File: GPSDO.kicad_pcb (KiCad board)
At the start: 2 copper layers, 85 x 85 mm, 100 parts, among them J1 Conn_Coaxial, J10 Conn_Coaxial, J2 Barrel_Jack, J3 PROG, J4 DISP_MODULE, J5 GPS_CONN, J6 Conn_Coaxial, J7 Conn_Coaxial, J8 Conn_Coaxial, J9 Conn_Coaxial, SW1 RESET_BTN, U1 REF3440IDBVR, U10 AVR32DB28x-xSO, U11 AZ1117H-5.0TRG1, U12 AZ1117H-5.0TRG1, U13 74HC390, U14 DS34C87T, U15 MCP6486T-E/OT, U2 74AUC2G04, U3 74AUC2G04, U4 74LVC2G74DP,125, U5 AD5680, U6 NB3N551MN, U7 74LVC1G125SE-7, U8 74LVC1G125SE-7, U9 LTC2050IS8, X1 OC5SC25

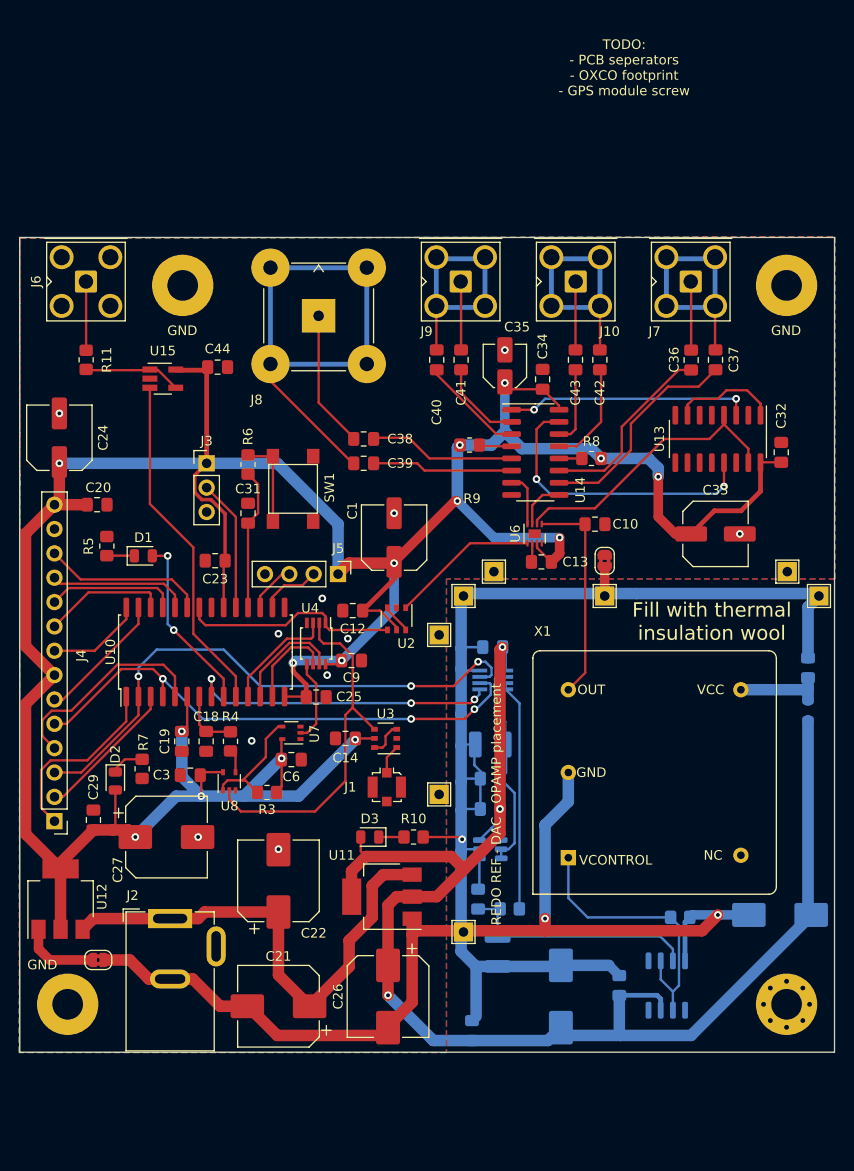
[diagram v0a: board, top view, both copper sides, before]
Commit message: changed flipflop & added vref
Flip-flop doesn't really benefit from having a set/reset that can be changed.
uC benefits from having an external reference. If not placed, internal one can be used.
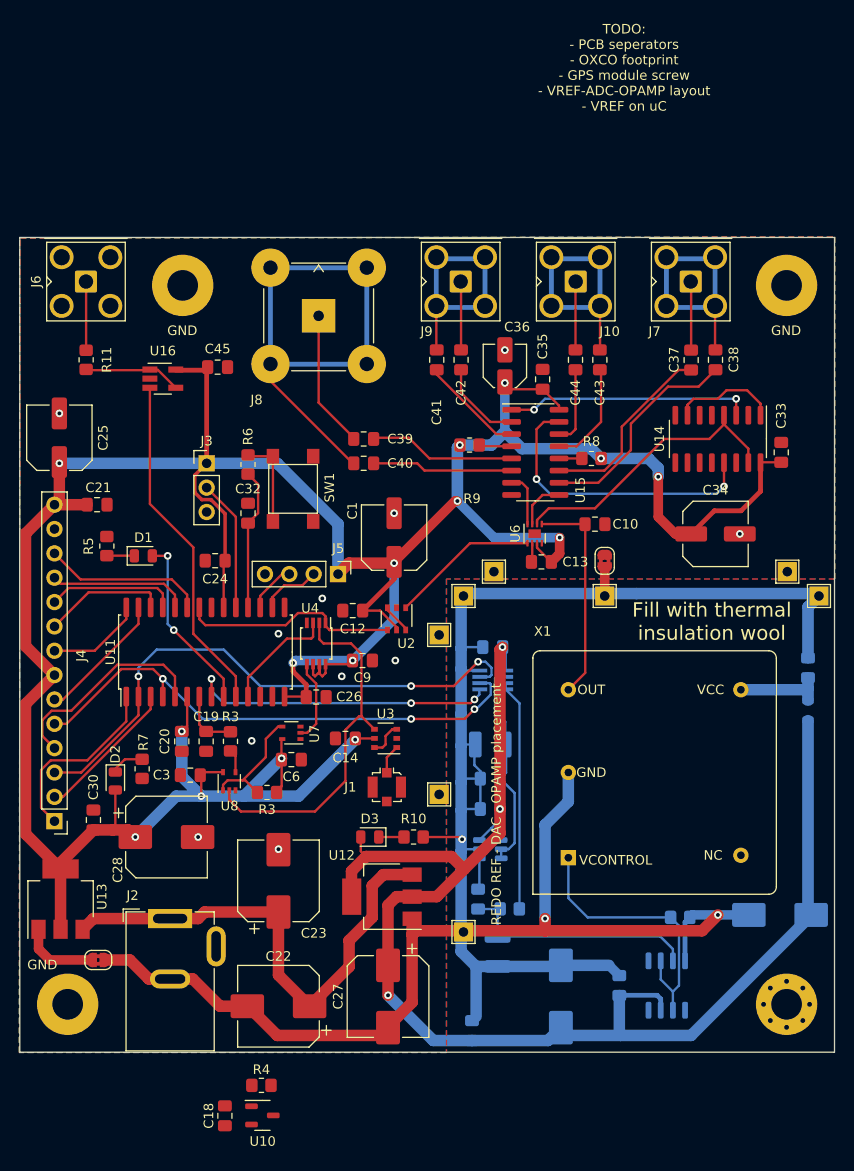
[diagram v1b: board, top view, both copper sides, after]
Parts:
- added C18: 10n, Capacitor_SMD:C_0805_2012Metric_Pad1.18x1.45mm_HandSolder, F.Cu at (41.4, 111.6)
- added R4: 270R, Resistor_SMD:R_0805_2012Metric_Pad1.20x1.40mm_HandSolder, F.Cu at (45.2, 108.5)
- added U10: LM4040AEX3-3.3+T, Package_TO_SOT_SMD:SOT-23-3, F.Cu at (45.3, 111.6)
- moved C9 1.14 mm to (55.8, 64.1)
- renumbered C18 to C19, C19 to C20, C20 to C21, C21 to C22, C22 to C23, C23 to C24, C24 to C25, C25 to C26, C26 to C27, C27 to C28, C28 to C29, C29 to C30, C30 to C31, C31 to C32, C32 to C33, C33 to C34, C34 to C35, C35 to C36, C36 to C37, C37 to C38, C38 to C39, C39 to C40, C40 to C41, C41 to C42, C42 to C43, C43 to C44, C44 to C45, R4 to R3, U10 to U11, U11 to U12, U12 to U13, U13 to U14, U14 to U15, U15 to U16
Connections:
- U11 pad 12: /FF_SET -> /UNUSED
- U11 pad 13: /FF_RESET -> /VREF_3V3
- U4 pad 6: /FF_RESET -> +5VD
- U4 pad 7: /FF_SET -> +5VD
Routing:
- net /FF_SET: track 11.6 -> 0.00 mm
- net /FF_RESET: track 9.66 -> 0.00 mm
- net +5VD: track 331.6 -> 338.7 mm
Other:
- board text added: "TODO: - PCB seperators - OXCO footprint - GPS module screw - VREF-ADC-OPAMP layout - VREF on uC"
- board text removed: "TODO: - PCB seperators - OXCO footprint - GPS module screw"

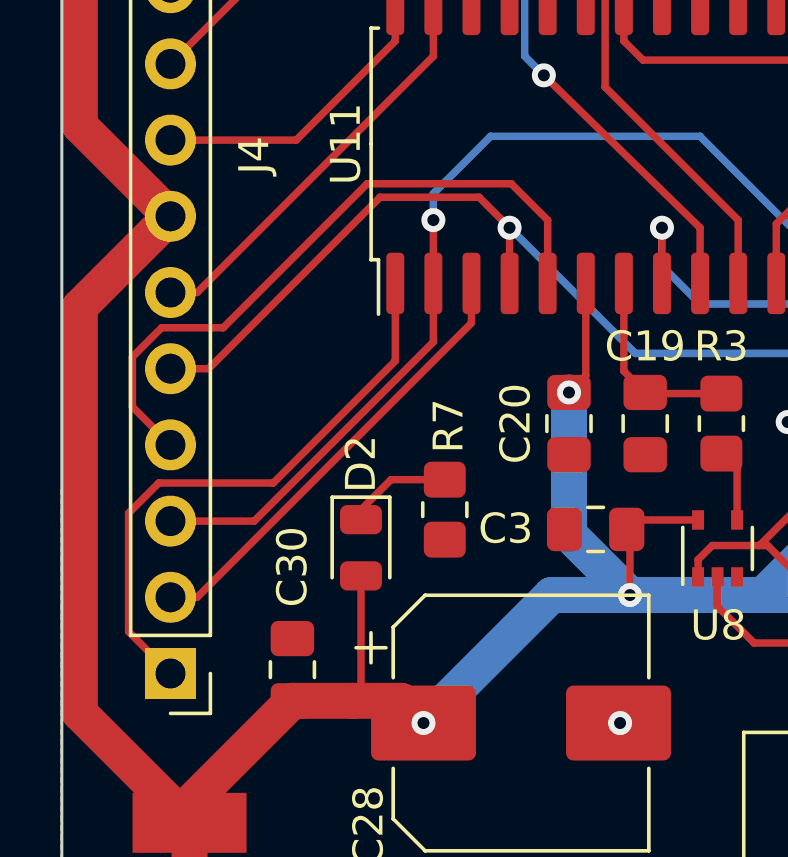
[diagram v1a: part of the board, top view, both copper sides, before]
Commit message: updated LCD layout
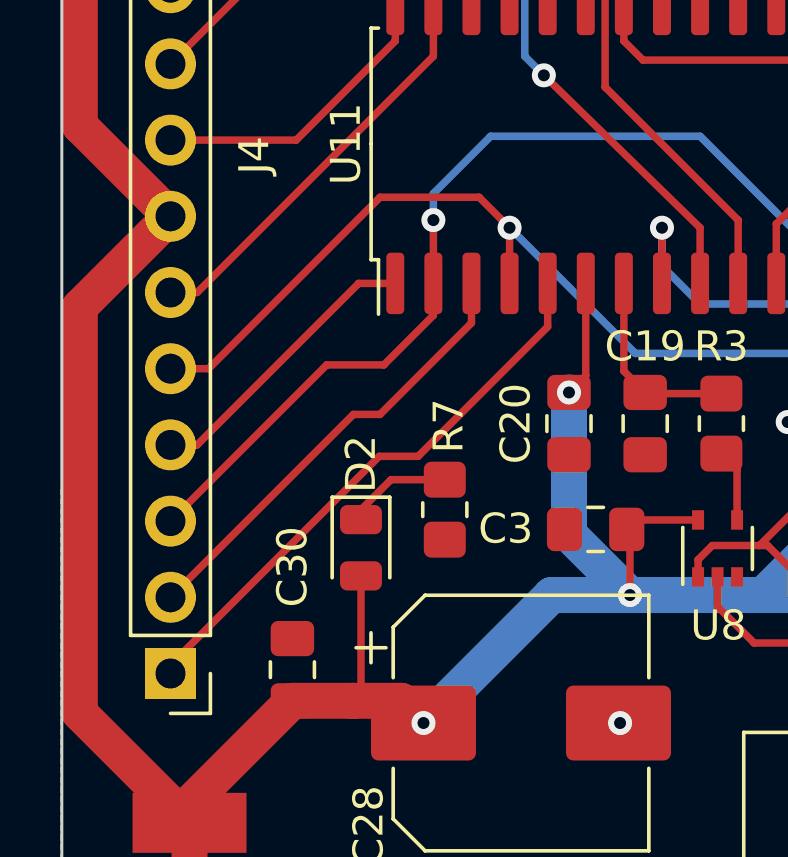
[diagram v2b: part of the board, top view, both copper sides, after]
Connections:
- U11 pad 1: /TOUCH_IRQ -> /~{TOUCH_SS}
- U11 pad 5: /~{TOUCH_SS} -> /TOUCH_IRQ
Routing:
- net /~{TOUCH_SS}: track 22.3 -> 9.72 mm
- net /TOUCH_IRQ: track 19.5 -> 19.0 mm
- net /DAC_MOSI: track 58.7 -> 58.2 mm
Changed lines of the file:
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@@
     (fp_line (start -2.75 -8.95) (end 3.75 -8.95) (layer "F.Fab") (width 0.1))
     (pad "1" smd roundrect (at -4.65 -8.255 90) (size 2.05 0.6) (layers "F.Cu" "F.Paste" "F.Mask") (roundrect_rratio 0.25)
-      (net 52 "/TOUCH_IRQ") (pinfunction "PA7") (pintype "bidirectional"))
+      (net 41 "/~{TOUCH_SS}") (pinfunction "PA7") (pintype "bidirectional"))
     (pad "2" smd roundrect (at -4.65 -6.985 90) (size 2.05 0.6) (layers "F.Cu" "F.Paste" "F.Mask") (roundrect_rratio 0.25)
       (net 26 "/DAC_MOSI") (pinfunction "PC0") (pintype "bidirectional"))
@@
       (net 42 "/DAC_SCK") (pinfunction "PC2") (pintype "bidirectional"))
     (pad "5" smd roundrect (at -4.65 -3.175 90) (size 2.05 0.6) (layers "F.Cu" "F.Paste" "F.Mask") (roundrect_rratio 0.25)
-      (net 41 "/~{TOUCH_SS}") (pinfunction "PC3") (pintype "bidirectional"))
+      (net 52 "/TOUCH_IRQ") (pinfunction "PC3") (pintype "bidirectional"))
     (pad "6" smd roundrect (at -4.65 -1.905 90) (size 2.05 0.6) (layers "F.Cu" "F.Paste" "F.Mask") (roundrect_rratio 0.25)
       (net 9 "+5VD") (pinfunction "VDDIO2") (pintype "power_in"))
@@
   (segment (start 65.278 66.802) (end 67.818 64.262) (width 0.25) (layer "F.Cu") (net 26))
   (segment (start 60.833 66.802) (end 65.278 66.802) (width 0.25) (layer "F.Cu") (net 26))
+  (segment (start 28.829 70.612) (end 30.734 70.612) (width 0.25) (layer "F.Cu") (net 26))
+  (segment (start 32.385 68.961) (end 32.385 67.896) (width 0.25) (layer "F.Cu") (net 26))
   (segment (start 32.385 67.896) (end 32.385 65.786) (width 0.25) (layer "F.Cu") (net 26))
-  (segment (start 32.385 67.896) (end 32.385 69.848604) (width 0.25) (layer "F.Cu") (net 26))
-  (segment (start 32.385 69.848604) (end 26.414604 75.819) (width 0.25) (layer "F.Cu") (net 26))
-  (segment (start 26.414604 75.819) (end 23.622 75.819) (width 0.25) (layer "F.Cu") (net 26))
+  (segment (start 23.622 75.819) (end 28.829 70.612) (width 0.25) (layer "F.Cu") (net 26))
+  (segment (start 30.734 70.612) (end 32.385 68.961) (width 0.25) (layer "F.Cu") (net 26))
   (via (at 67.818 64.262) (size 0.8) (drill 0.4) (layers "F.Cu" "B.Cu") (net 26))
   (via (at 60.833 66.802) (size 0.8) (drill 0.4) (layers "F.Cu" "B.Cu") (net 26))
@@
   (segment (start 42.545 49.149) (end 42.545 58.596) (width 0.25) (layer "F.Cu") (net 40))
   (segment (start 39.497 46.101) (end 42.545 49.149) (width 0.25) (layer "F.Cu") (net 40))
-  (segment (start 36.195 65.786) (end 34.983 64.574) (width 0.25) (layer "F.Cu") (net 41))
-  (segment (start 36.195 67.896) (end 36.195 65.786) (width 0.25) (layer "F.Cu") (net 41))
-  (segment (start 23.325299 69.374) (end 22.352 70.347299) (width 0.25) (layer "F.Cu") (net 41))
-  (segment (start 25.378701 69.374) (end 23.325299 69.374) (width 0.25) (layer "F.Cu") (net 41))
-  (segment (start 22.352 72.009) (end 23.622 73.279) (width 0.25) (layer "F.Cu") (net 41))
-  (segment (start 30.178701 64.574) (end 25.378701 69.374) (width 0.25) (layer "F.Cu") (net 41))
-  (segment (start 22.352 70.347299) (end 22.352 72.009) (width 0.25) (layer "F.Cu") (net 41))
-  (segment (start 34.983 64.574) (end 30.178701 64.574) (width 0.25) (layer "F.Cu") (net 41))
+  (segment (start 23.622 73.279) (end 24.511 73.279) (width 0.25) (layer "F.Cu") (net 41))
+  (segment (start 24.511 73.279) (end 29.894 67.896) (width 0.25) (layer "F.Cu") (net 41))
+  (segment (start 29.894 67.896) (end 31.115 67.896) (width 0.25) (layer "F.Cu") (net 41))
   (segment (start 23.622 70.739) (end 24.892 70.739) (width 0.25) (layer "F.Cu") (net 42))
   (segment (start 60.833 70.231) (end 66.421 70.231) (width 0.25) (layer "F.Cu") (net 42))
@@
   (segment (start 29.972 75.7705) (end 29.972 75.438) (width 0.25) (layer "F.Cu") (net 51))
   (segment (start 30.972 74.438) (end 32.766 74.438) (width 0.25) (layer "F.Cu") (net 51))
-  (segment (start 23.230299 74.549) (end 22.225 75.554299) (width 0.25) (layer "F.Cu") (net 52))
-  (segment (start 27.048208 74.549) (end 23.230299 74.549) (width 0.25) (layer "F.Cu") (net 52))
-  (segment (start 31.115 70.482208) (end 27.048208 74.549) (width 0.25) (layer "F.Cu") (net 52))
-  (segment (start 31.115 67.896) (end 31.115 70.482208) (width 0.25) (layer "F.Cu") (net 52))
-  (segment (start 22.225 75.554299) (end 22.225 79.502) (width 0.25) (layer "F.Cu") (net 52))
-  (segment (start 22.225 79.502) (end 23.622 80.899) (width 0.25) (layer "F.Cu") (net 52))
+  (segment (start 36.195 69.342) (end 36.195 67.896) (width 0.25) (layer "F.Cu") (net 52))
+  (segment (start 23.622 80.616166) (end 30.578166 73.66) (width 0.25) (layer "F.Cu") (net 52))
+  (segment (start 30.578166 73.66) (end 31.877 73.66) (width 0.25) (layer "F.Cu") (net 52))
+  (segment (start 31.877 73.66) (end 36.195 69.342) (width 0.25) (layer "F.Cu") (net 52))
+  (segment (start 23.622 80.899) (end 23.622 80.616166) (width 0.25) (layer "F.Cu") (net 52))
   (segment (start 58.293 75.462) (end 58.293 74.246) (width 0.25) (layer "F.Cu") (net 53))
   (segment (start 58.293 74.246) (end 59.326 73.213) (width 0.25) (layer "F.Cu") (net 53))
@@
   (segment (start 93.472 45.974) (end 92.71 46.736) (width 0.25) (layer "B.Cu") (net 59))
   (segment (start 75.311 46.736) (end 73.914 45.339) (width 0.25) (layer "B.Cu") (net 59))
-  (segment (start 33.655 69.215) (end 24.511 78.359) (width 0.25) (layer "F.Cu") (net 60))
-  (segment (start 33.655 67.896) (end 33.655 69.215) (width 0.25) (layer "F.Cu") (net 60))
-  (segment (start 24.511 78.359) (end 23.622 78.359) (width 0.25) (layer "F.Cu") (net 60))
+  (segment (start 29.718 72.263) (end 30.607 72.263) (width 0.25) (layer "F.Cu") (net 60))
+  (segment (start 30.607 72.263) (end 33.655 69.215) (width 0.25) (layer "F.Cu") (net 60))
+  (segment (start 33.655 69.215) (end 33.655 67.896) (width 0.25) (layer "F.Cu") (net 60))
+  (segment (start 23.622 78.359) (end 29.718 72.263) (width 0.25) (layer "F.Cu") (net 60))
   (segment (start 31.115 59.817) (end 27.813 63.119) (width 0.25) (layer "F.Cu") (net 61))
   (segment (start 31.115 58.596) (end 31.115 59.817) (width 0.25) (layer "F.Cu") (net 61))

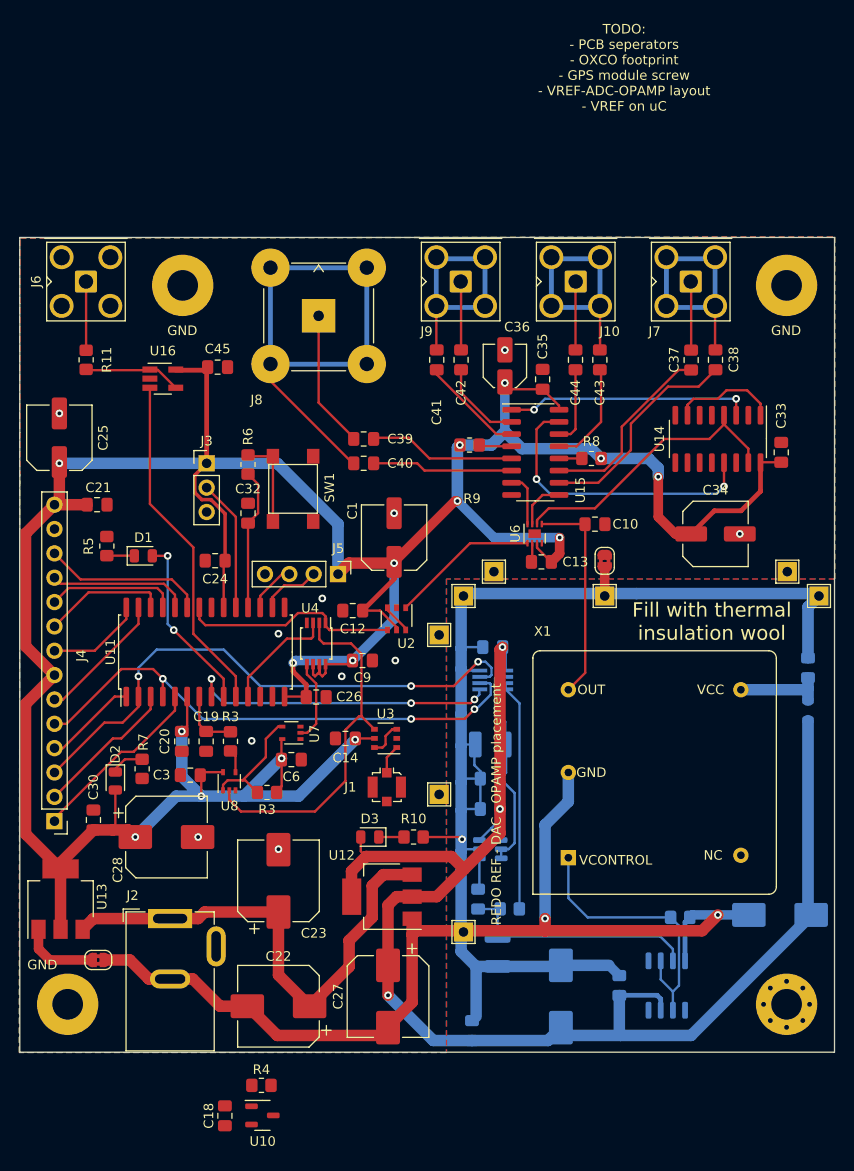
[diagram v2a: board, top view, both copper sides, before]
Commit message: updated layout
Added vref footprint
Changed pour params for better gnd coverage
increased digital line distances
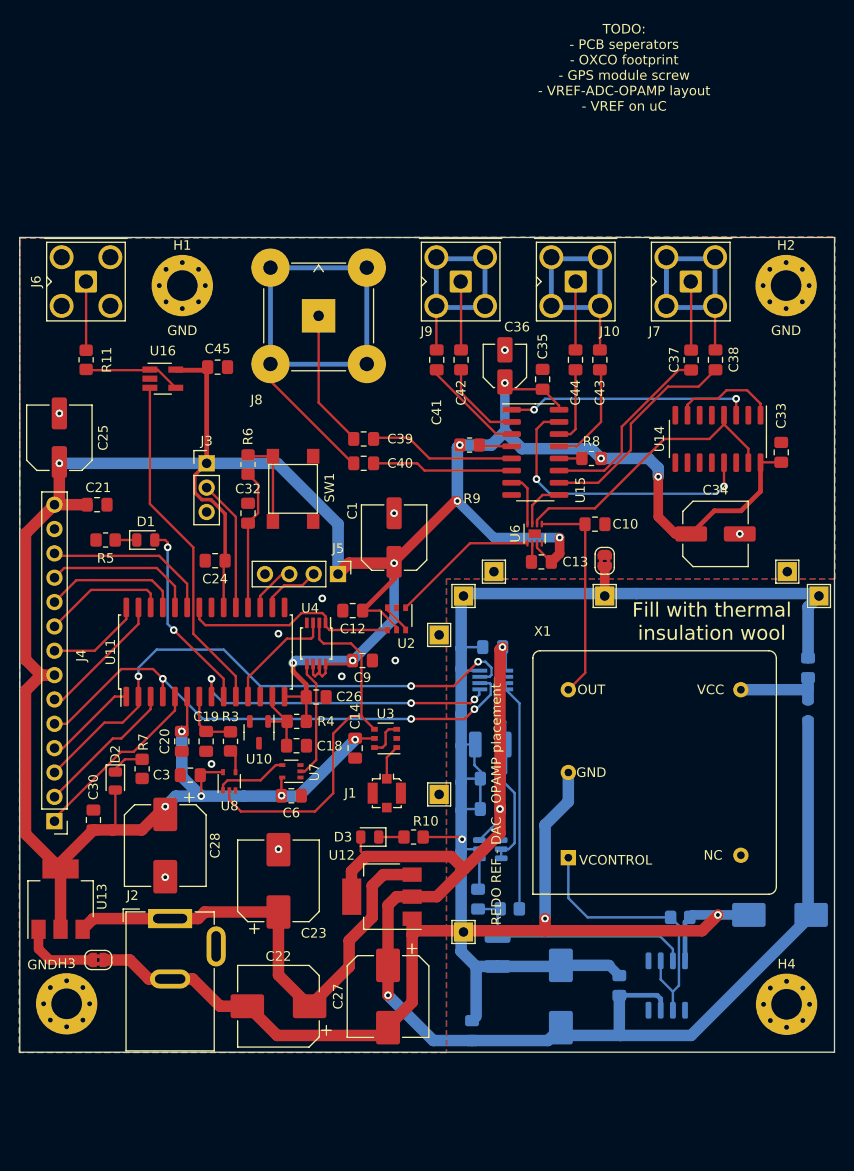
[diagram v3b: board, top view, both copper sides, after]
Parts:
- removed the R3 at (45.8, 77.9)
- H1, H2, H3: value MountingHole -> Hole; footprint MountingHole:MountingHole_3.2mm_M3_Pad -> MountingHole:MountingHole_3.2mm_M3_Pad_Via
- H4: value MountingHole -> Hole
- moved H1 75.9 mm to (37.0, 25.0)
- moved H3 75.9 mm to (24.9, 99.9)
- moved U10 40.0 mm to (45.0, 71.6), turned to -90 degrees
- moved C18 39.3 mm to (48.9, 73.0), turned to 180 degrees
- moved R4 38.2 mm to (48.9, 70.5)
- moved U7 4.01 mm to (48.3, 75.7)
- moved C6 3.77 mm to (48.3, 78.2)
- moved D1 1.67 mm to (33.1, 51.6)
- moved C14 1.44 mm to (55.0, 73.3), turned to 90 degrees
- moved C28 0.90 mm to (35.2, 83.4), turned to -90 degrees
- moved R5 0.65 mm to (29.0, 51.6), turned to 0 degrees
- moved J1 0.63 mm to (58.3, 78.0)
- moved H2 0.05 mm to (99.9, 25.0)
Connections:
- H1 pad 1: (no net) -> GND
- H2 pad 1: (no net) -> GND
- H3 pad 1: (no net) -> GND
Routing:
- net /VREF_3V3: track 0.00 -> 7.78 mm
- net +5VD: track 338.7 -> 331.4 mm
- net Net-(U7-Pad4): track 12.5 -> 7.61 mm
- net Net-(U4-Pad5): track 8.67 -> 12.5 mm
- net /LCD_RESET: track 14.6 -> 16.0 mm
- net Net-(D1-Pad2): track 18.7 -> 20.0 mm
- net /PPS_SIG_3V3: track 2.68 -> 3.69 mm
- net /LCD_DCRS: track 13.6 -> 14.4 mm
- net /~{LCD_SS}: track 17.0 -> 17.6 mm
- net Net-(D1-Pad1): track 2.88 -> 2.25 mm
- net /PPS_SIG: track 37.7 -> 38.2 mm

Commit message: Re-layout of Vref-OPAMP-DAC
made analog connections shorter
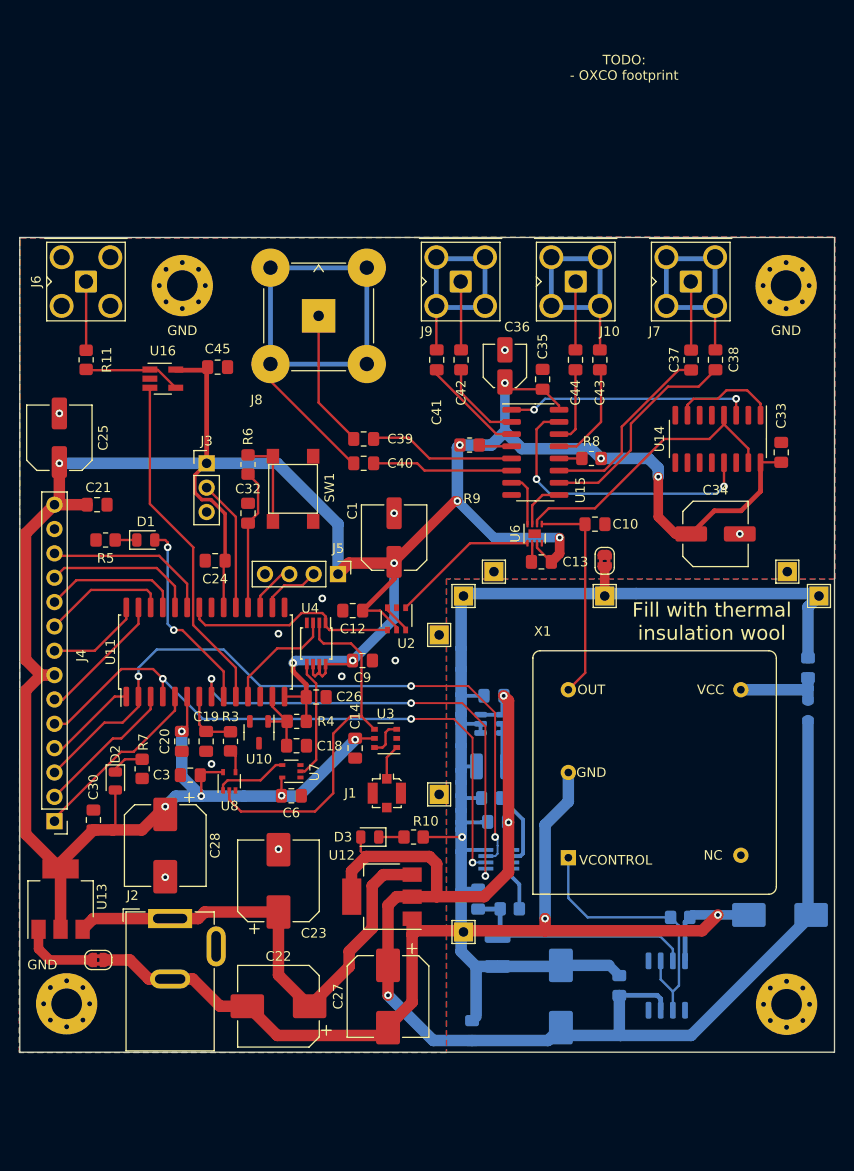
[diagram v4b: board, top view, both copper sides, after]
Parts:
- moved U5 18.7 mm to (70.0, 84.9)
- moved C11 18.2 mm to (69.8, 81.0)
- moved U1 13.1 mm to (69.2, 70.7)
- moved C4 11.8 mm to (69.5, 67.8)
- moved C8 2.29 mm to (69.2, 75.2)
- moved C5 2.04 mm to (69.2, 78.5)
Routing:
- net Net-(R2-Pad1): track 24.2 -> 5.47 mm
- net /~{DAC_SS}: track 32.5 -> 49.6 mm
- net /DAC_MOSI: track 58.2 -> 72.5 mm
- net /DAC_SCK: track 55.3 -> 65.3 mm
- net GNDA: track 242.8 -> 234.9 mm
- net Net-(C5-Pad1): track 22.3 -> 16.1 mm
- net +5VA: track 152.5 -> 150.2 mm
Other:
- board text added: "TODO: - OXCO footprint"
- board text removed: "REDO REF - DAC - OPAMP placement"
- board text removed: "TODO: - PCB seperators - OXCO footprint - GPS module screw - VREF-ADC-OPAMP layout - VREF on uC"
